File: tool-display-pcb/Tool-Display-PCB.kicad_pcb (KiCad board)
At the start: 2 copper layers, 43.6 x 54.6 mm, 4 parts, among them J1 DISPLAY, J2 ESP32 30-Pin

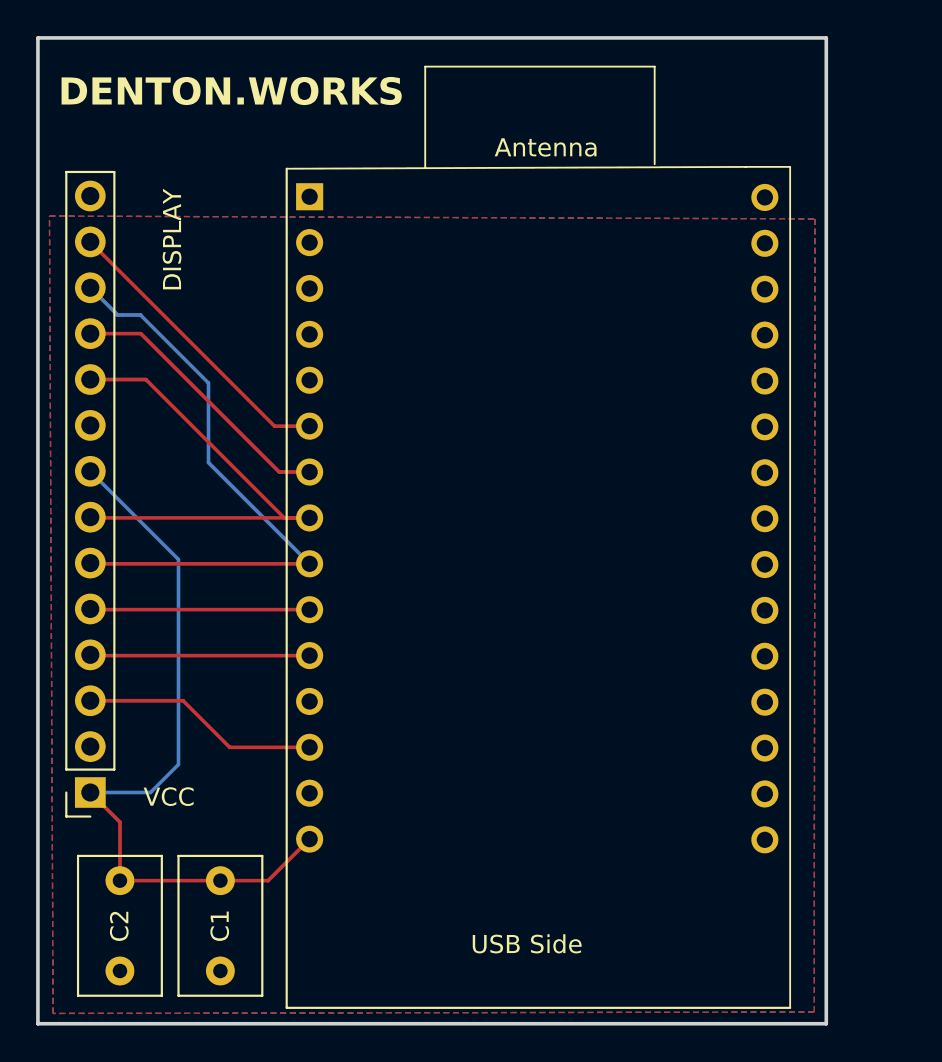
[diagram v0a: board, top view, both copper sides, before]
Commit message: PCB updates, narrower, additional USB option
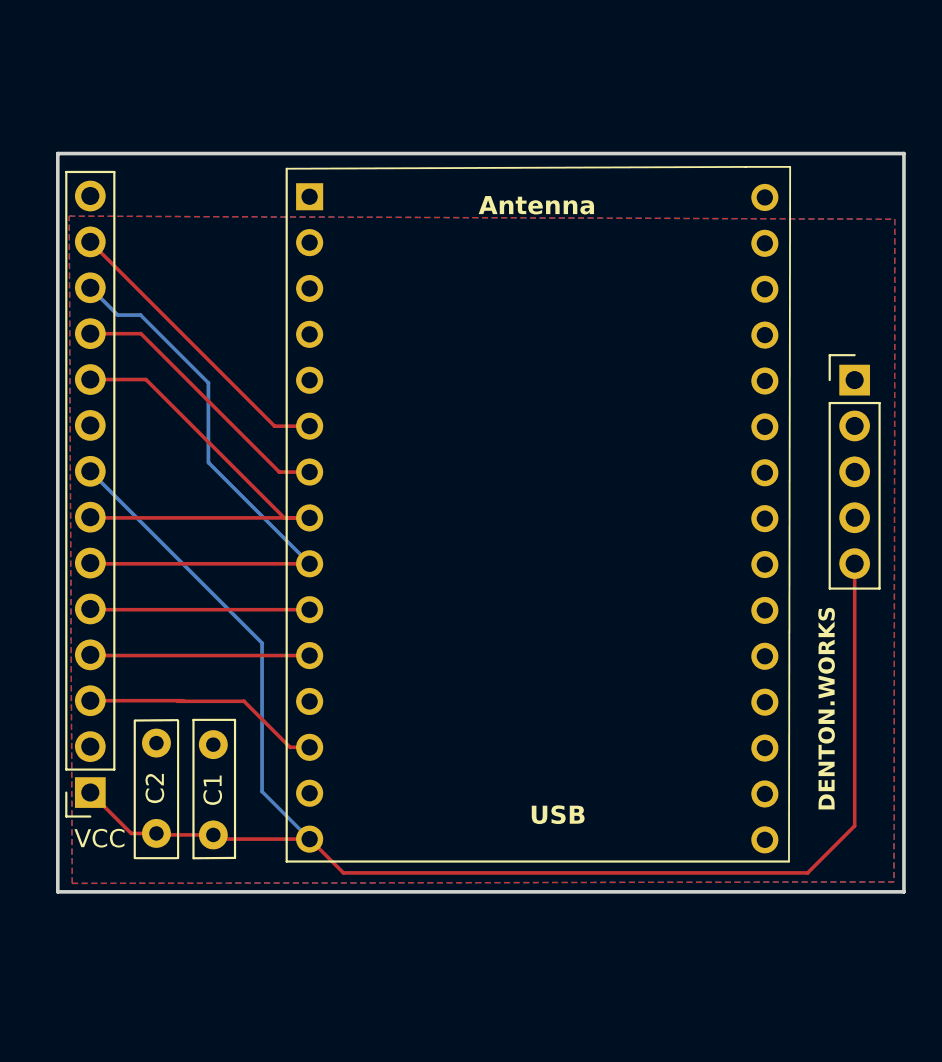
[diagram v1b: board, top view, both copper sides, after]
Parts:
- added J4: Conn_01x05_Pin, Connector_PinHeader_2.54mm:Alex-5pin-microUSB, F.Cu at (145.1, 74.8)
- J1: value DISPLAY -> 4" TFT SPI DISPLAY
- moved C2 12.8 mm to (106.5, 94.9), turned to -90 degrees
- moved C1 12.5 mm to (109.6, 95.0), turned to -90 degrees
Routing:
- net Net-(J1-Pin_1): track 40.8 -> 85.1 mm
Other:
- board size 43.6 x 54.6 mm -> 46.8 x 40.9 mm
